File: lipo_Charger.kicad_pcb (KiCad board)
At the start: 2 copper layers, 98 parts, among them J1 Conn_01x02_Pin, J2 Conn_01x05, J3 Conn_01x04, J4 Conn_01x05, J5 Conn_01x04, Q1 NX7002AK_215(nch low power), Q2 NVTFS010N10MCLTAG(high power), Q3 NVTFS010N10MCLTAG(high power), Q4 NVTFS010N10MCLTAG(high power), Q5 NVTFS010N10MCLTAG(high power)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

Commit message: need to add stm dev boarrd and silkscreen managing sch rechecik and trace width check eed to add gnd and power plane
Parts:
- moved C24 83.7 mm to (120.6, 66.9)
- moved R4 83.7 mm to (108.5, 70.7)
- moved R40 83.7 mm to (143.1, 86.7)
- moved C1 83.7 mm to (85.9, 62.9)
- moved C15 83.7 mm to (144.8, 60.3)
- moved C16 83.7 mm to (147.9, 60.3)
- moved C18 83.7 mm to (155.0, 70.5)
- moved C2 83.7 mm to (88.9, 62.9)
- moved C21 83.7 mm to (129.7, 66.2)
- moved C22 83.7 mm to (111.5, 76.3)
- moved C23 83.7 mm to (105.1, 76.3)
- moved C27 83.7 mm to (116.2, 76.9)
- moved C3 83.7 mm to (91.9, 62.9)
- moved C33 83.7 mm to (146.2, 84.9)
- moved C4 83.7 mm to (94.9, 62.9)
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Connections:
- net Net-(Q2-Pad5-6-7-8) renamed /copper_pour1
- net Net-(U1-SW2) renamed /copper_pour2
- MOSFET2 pad 5: Net-(MOSFET2-D-Pad5) -> /copper_pour3
- Q3 pad 5-6-7-8: Net-(MOSFET2-D-Pad5) -> /copper_pour3
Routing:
- net +24V: track 40.2 -> 2.50 mm
- net /BAT: track 54.8 -> 70.8 mm
- net /copper_pour2: track 47.7 -> 37.5 mm
- net GND: track 43.5 -> 35.1 mm
- net /copper_pour1: track 9.91 -> 2.42 mm
- net Net-(MOSFET2-D-Pad5): track 5.88 -> 0.00 mm
- net /VSYS: track 39.9 -> 43.6 mm
- net /CELL_3S: track 57.7 -> 60.0 mm
- net /CELL_1S: track 69.0 -> 70.8 mm
- net /CELL_2S: track 62.4 -> 64.2 mm
- net Net-(MOSFET5-D-Pad5): track 7.35 -> 9.13 mm
- net Net-(MOSFET4-D-Pad5): track 6.75 -> 8.53 mm
- net Net-(MOSFET3-D-Pad5): track 5.65 -> 7.38 mm
- net Net-(U1-HIDRV1): track 7.70 -> 8.90 mm
- net Net-(U1-CELL_BATPRES): track 24.7 -> 23.8 mm
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- added copper zone on F.Cu, net +24V
- added copper zone on F.Cu, net /copper_pour1
- added copper zone on F.Cu, net /copper_pour2
- added copper zone on F.Cu, net /copper_pour3
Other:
- copper layers 2 -> 4

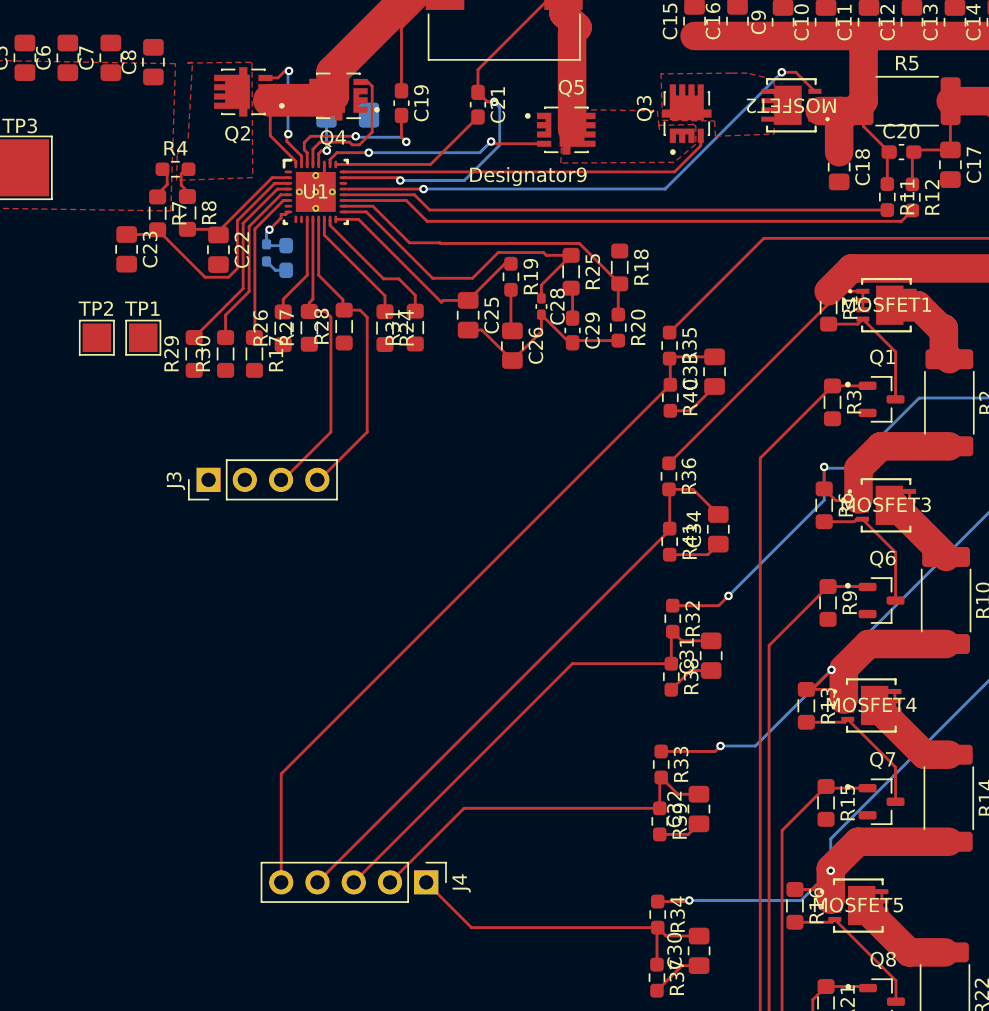
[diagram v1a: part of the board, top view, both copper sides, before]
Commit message: need to seperate analog and digital ground and reroute everything
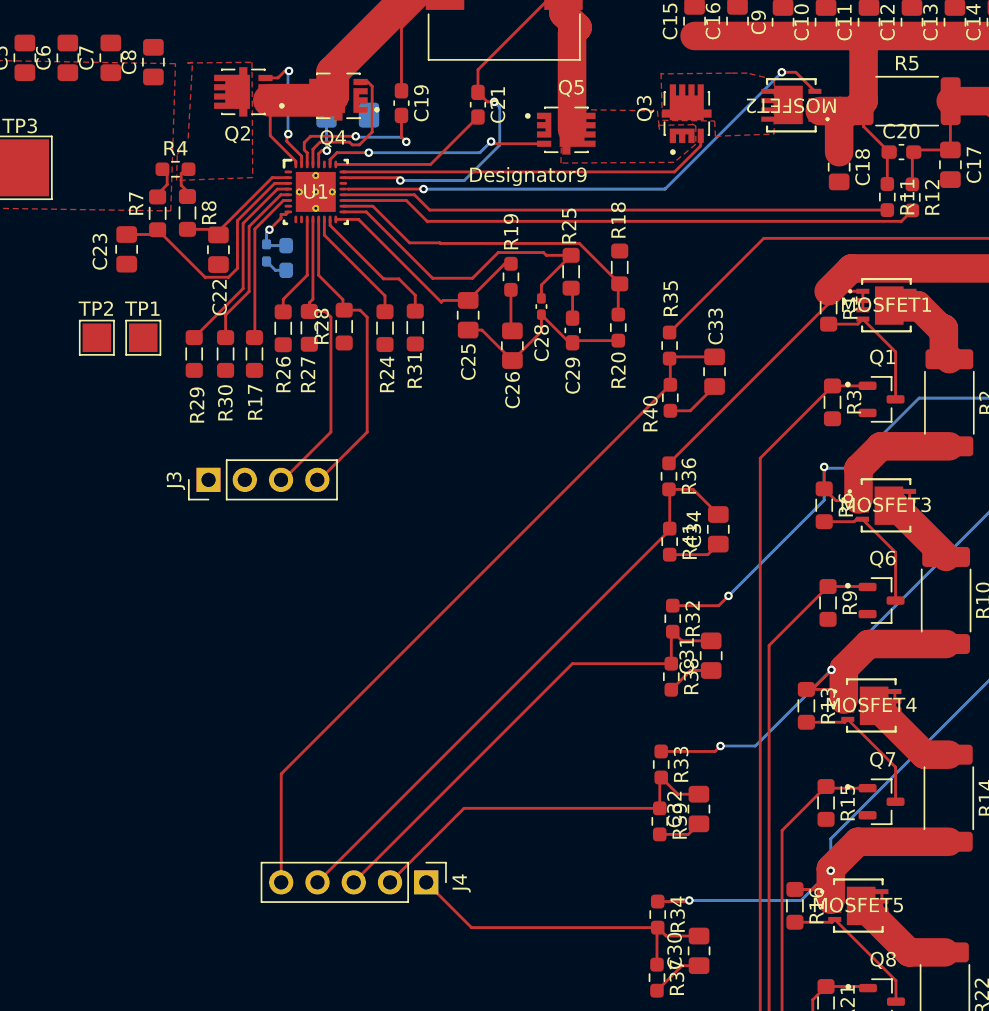
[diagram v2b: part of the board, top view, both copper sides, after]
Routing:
- net GND: track 35.1 -> 33.8 mm
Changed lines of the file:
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@@
 		(tags "inductor handsolder")
 		(property "Reference" "R30"
-			(at 0 -1.55 90)
+			(at -3.4426 0.021 90)
 			(layer "F.SilkS")
 			(effects
@@
 		)
 		(fp_text user "${REFERENCE}"
-			(at 0 0 90)
+			(at 0 0.1226 90)
 			(layer "F.Fab")
 			(effects
@@
 		(tags "inductor handsolder")
 		(property "Reference" "R18"
-			(at 0 -1.55 90)
+			(at -3.2961 0.0546 90)
 			(layer "F.SilkS")
 			(effects
@@
 		)
 		(pad "5" smd rect
-			(at 0.233775 0)
-			(size 1.92005 2.749999)
+			(at 0.2 0.025)
+			(size 2.0066 2.6924)
 			(layers "F.Cu" "F.Mask" "F.Paste")
 			(net 28 "Net-(MOSFET3-D-Pad5)")
@@
 		(tags "resistor handsolder")
 		(property "Reference" "R35"
-			(at 0 -1.43 90)
+			(at -3.2844 -0.1095 90)
 			(layer "F.SilkS")
 			(effects
@@
 		(tags "inductor handsolder")
 		(property "Reference" "R17"
-			(at 0 -1.55 90)
+			(at 3.3918 -0.0838 90)
 			(layer "F.SilkS")
 			(effects
@@
 		(tags "capacitor handsolder")
 		(property "Reference" "C28"
-			(at 0 -1.16 90)
+			(at 2.5478 -0.047 90)
 			(layer "F.SilkS")
 			(effects
@@
 		(tags "inductor handsolder")
 		(property "Reference" "R24"
-			(at 0 -1.55 90)
+			(at 3.2714 -0.1826 90)
 			(layer "F.SilkS")
 			(effects
@@
 		(tags "inductor handsolder")
 		(property "Reference" "R7"
-			(at 0 -1.55 90)
+			(at -0.6774 1.4674 90)
 			(layer "F.SilkS")
 			(effects
@@
 		(tags "capacitor handsolder")
 		(property "Reference" "C22"
-			(at 0 -1.68 90)
+			(at 3.3258 -0.1146 90)
 			(layer "F.SilkS")
 			(effects
@@
 		(tags "capacitor handsolder")
 		(property "Reference" "C26"
-			(at 0 -1.68 90)
+			(at 3.1066 -0.047 90)
 			(layer "F.SilkS")
 			(effects
@@
 		(tags "resistor handsolder")
 		(property "Reference" "R19"
-			(at 0 -1.43 90)
+			(at -3.1418 -0.047 90)
 			(layer "F.SilkS")
 			(effects
@@
 		)
 		(pad "5" smd rect
-			(at 0.233775 0)
-			(size 1.92005 2.749999)
+			(at 0.2 0.025)
+			(size 2.0066 2.6924)
 			(layers "F.Cu" "F.Mask" "F.Paste")
 			(net 30 "Net-(MOSFET4-D-Pad5)")
@@
 		(tags "inductor handsolder")
 		(property "Reference" "R31"
-			(at 0 -1.55 90)
+			(at -3.0066 -0.007 90)
 			(layer "F.SilkS")
 			(effects
@@
 		)
 		(pad "5" smd rect
-			(at 0.233775 0 180)
-			(size 1.92005 2.749999)
+			(at 0.2 0.025 180)
+			(size 2.0066 2.6924)
 			(layers "F.Cu" "F.Mask" "F.Paste")
 			(net 58 "/copper_pour3")
@@
 		(tags "inductor handsolder")
 		(property "Reference" "R25"
-			(at 0 -1.55 90)
+			(at -3.1926 0.1054 90)
 			(layer "F.SilkS")
 			(effects
@@
 		(tags "inductor handsolder")
 		(property "Reference" "R29"
-			(at 0 -1.55 90)
+			(at -3.595 0.2398 90)
 			(layer "F.SilkS")
 			(effects
@@
 		)
 		(pad "5" smd rect
-			(at 0.233775 0)
-			(size 1.92005 2.749999)
+			(at 0.2 0.025)
+			(size 2.0066 2.6924)
 			(layers "F.Cu" "F.Mask" "F.Paste")
 			(net 25 "Net-(MOSFET1-D-Pad5)")
@@
 		(tags "capacitor handsolder")
 		(property "Reference" "C23"
-			(at 0 -1.68 90)
+			(at 0.1554 1.8374 90)
 			(layer "F.SilkS")
 			(effects
@@
 		(tags "resistor handsolder")
 		(property "Reference" "R20"
-			(at 0 -1.43 90)
+			(at 3.0031 -0.047 90)
 			(layer "F.SilkS")
 			(effects
@@
 		(tags "capacitor handsolder")
 		(property "Reference" "C25"
-			(at 0 -1.68 90)
+			(at 3.259 -0.047 90)
 			(layer "F.SilkS")
 			(effects
@@
 		(tags "inductor handsolder")
 		(property "Reference" "R26"
-			(at 0 -1.55 90)
+			(at -3.259 0.047 90)
 			(layer "F.SilkS")
 			(effects
@@
 		)
 		(pad "5" smd rect
-			(at 0.233775 0)
-			(size 1.92005 2.749999)
+			(at 0.2 0.025)
+			(size 2.0066 2.6924)
 			(layers "F.Cu" "F.Mask" "F.Paste")
 			(net 31 "Net-(MOSFET5-D-Pad5)")
@@
 		(tags "inductor handsolder")
 		(property "Reference" "R27"
-			(at 0 -1.55 90)
+			(at -3.2914 -0.0546 90)
 			(layer "F.SilkS")
 			(effects
@@
 		(tags "capacitor handsolder")
 		(property "Reference" "C29"
-			(at 0 -1.43 90)
+			(at 3.1574 -0.047 90)
 			(layer "F.SilkS")
 			(effects
@@
 		(tags "capacitor handsolder")
 		(property "Reference" "C33"
-			(at 0 -1.68 90)
+			(at 3.1828 0.1095 90)
 			(layer "F.SilkS")
 			(effects
@@
 		(tags "resistor handsolder")
 		(property "Reference" "R40"
-			(at 0 -1.43 90)
+			(at 1.1352 1.3637 90)
 			(layer "F.SilkS")
 			(effects
@@
 		(width 0.2)
 		(layer "F.Cu")
-		(net 1)
-	)
-	(segment
-		(start 118.913001 70.3536)
-		(end 118.913001 71.678602)
-		(width 0.2)
-		(layer "F.Cu")

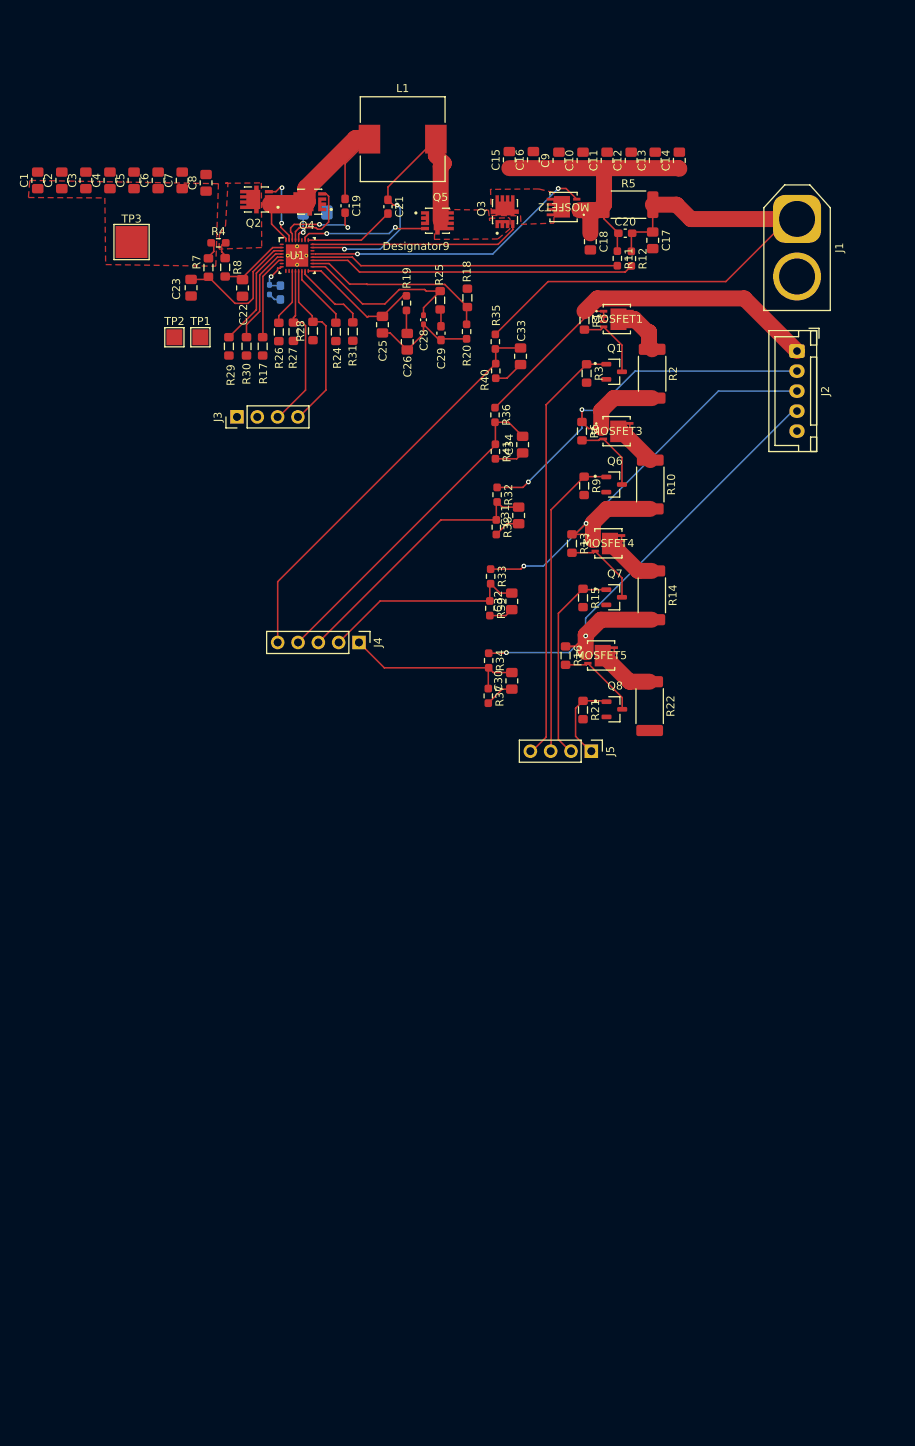
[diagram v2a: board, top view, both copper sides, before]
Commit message: all the links of the components has been assigned in the library for routing components placement is optimizes need routing
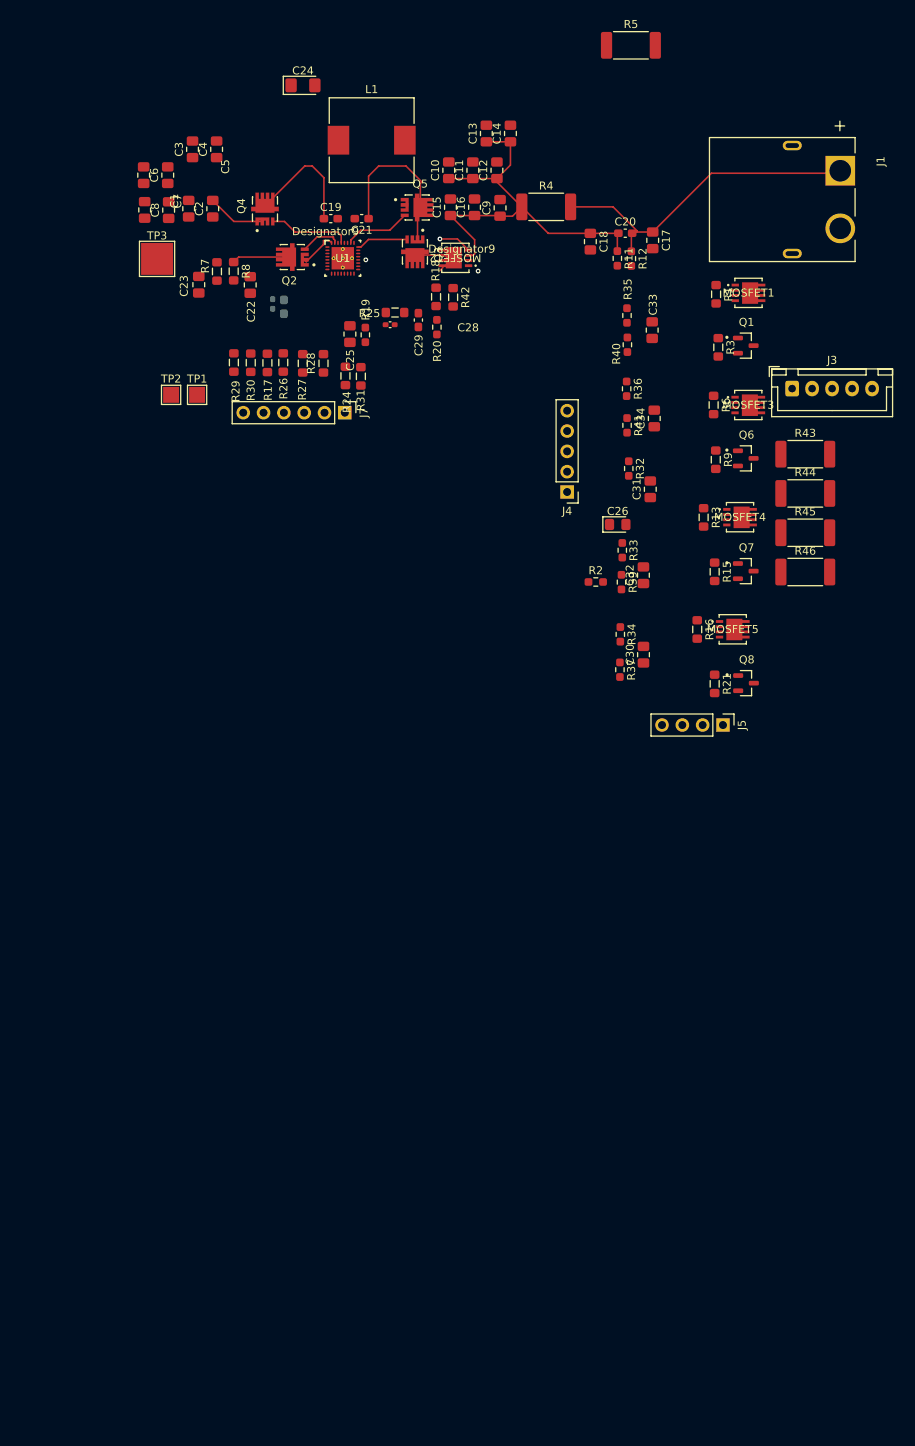
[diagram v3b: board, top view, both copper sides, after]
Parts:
- removed J2: Conn_01x05, Connector_JST:JST_XH_B5B-XH-A_1x05_P2.50mm_Vertical
- removed R10, R14, R22: R, Resistor_SMD:R_2512_6332Metric_Pad1.40x3.35mm_HandSolder
- removed R38: 8.2k, Resistor_SMD:R_0603_1608Metric_Pad0.98x0.95mm_HandSolder
- added J7: Conn_01x07, Connector_PinHeader_2.54mm:PinHeader_1x06_P2.54mm_Vertical, F.Cu at (124.3, 91.9)
- added R42: 10k, Inductor_SMD:L_0805_2012Metric_Pad1.05x1.20mm_HandSolder, F.Cu at (137.8, 77.5)
- added R43: 47ohm, Resistor_SMD:R_2512_6332Metric_Pad1.40x3.35mm_HandSolder, F.Cu at (181.8, 97.1)
- added R44: 47ohm, Resistor_SMD:R_2512_6332Metric_Pad1.40x3.35mm_HandSolder, F.Cu at (181.8, 102.0)
- added R45: 47ohm, Resistor_SMD:R_2512_6332Metric_Pad1.40x3.35mm_HandSolder, F.Cu at (181.8, 106.9)
- added R46: 47ohm, Resistor_SMD:R_2512_6332Metric_Pad1.40x3.35mm_HandSolder, F.Cu at (181.8, 111.8)
- C24: moved to F.Cu
- C26: footprint Capacitor_SMD:C_0805_2012Metric_Pad1.18x1.45mm_HandSolder -> Diode_SMD:D_0805_2012Metric_Pad1.15x1.40mm_HandSolder
- J1: value Conn_01x02_Pin -> XT60PW-M; footprint Connector_AMASS:AMASS_XT60-M_1x02_P7.20mm_Vertical -> Lipo_Charger_footprint:AMASS_XT60PW-M
- J3: value Conn_01x04 -> balance_plug_4s; footprint Connector_PinHeader_2.54mm:PinHeader_1x04_P2.54mm_Vertical -> Connector_JST:JST_XH_B5B-XH-A_1x05_P2.50mm_Vertical
- R2: value R -> 8.2k; footprint Resistor_SMD:R_2512_6332Metric_Pad1.40x3.35mm_HandSolder -> Resistor_SMD:R_0603_1608Metric_Pad0.98x0.95mm_HandSolder
- R4: value R(10ohm) -> 0.01ohm; footprint Resistor_SMD:R_0603_1608Metric_Pad0.98x0.95mm_HandSolder -> Resistor_SMD:R_2512_6332Metric_Pad1.40x3.35mm_HandSolder
- R5: value R -> 0.01ohm
- moved J3 69.5 mm to (180.2, 88.9), turned to 0 degrees
- moved R4 41.2 mm to (149.5, 66.2)
- moved C26 34.8 mm to (158.4, 105.9), turned to 0 degrees
- moved J4 32.1 mm to (152.1, 101.8), turned to 180 degrees
- moved R2 27.0 mm to (155.7, 113.1), turned to 0 degrees
- moved C13 21.4 mm to (142.0, 57.0)
- moved C14 21.4 mm to (145.0, 57.0)
- moved R5 19.9 mm to (160.0, 46.0)
- moved C1 19.2 mm to (104.8, 66.4)
- moved C2 19.2 mm to (107.8, 66.4)
- moved C11 16.8 mm to (140.3, 61.6)
- moved C12 16.8 mm to (143.3, 61.6)
- moved C10 16.8 mm to (137.3, 61.6)
- moved C30 16.8 mm to (161.6, 122.2)
- moved C33 16.8 mm to (162.7, 81.6)
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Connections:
- C22 pad 2: GND -> GNDA
- C23 pad 2: GND -> GNDA
- C24 pad 2: GND -> GNDA
- C25 pad 2: GND -> GNDA
- C26 pad 2: GND -> GNDA
- C27 pad 2: GND -> GNDA
- C28 pad 2: GND -> GNDA
- C29 pad 2: GND -> GNDA
- C31 pad 1: GND -> GNDA
- C32 pad 1: GND -> GNDA
- C33 pad 1: GND -> GNDA
- C34 pad 1: GND -> GNDA
- J3 pad 1: GND -> /CELL_4S
- J3 pad 2: VDDA -> /CELL_3S
- J3 pad 3: /SCL -> /CELL_2S
- J3 pad 4: /SDA -> /CELL_1S
- R17 pad 2: GND -> GNDA
- R2 pad 1: Net-(MOSFET1-D-Pad5) -> /CELL_3S_adc
- R2 pad 2: /CELL_3S -> GNDA
- R20 pad 2: GND -> GNDA
- R23 pad 2: GND -> GNDA
- R24 pad 2: GND -> GNDA
- R39 pad 2: GND -> GNDA
- R4 pad 1: +24V -> /VSYS
- R4 pad 2: /copper_pour1 -> /BAT
- R40 pad 2: GND -> GNDA
- R41 pad 2: GND -> GNDA
- R5 pad 1: /VSYS -> +24V
- R5 pad 2: /BAT -> /copper_pour1
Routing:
- net /CELL_1S: track 70.8 -> 0.00 mm, vias 2 -> 0
- net /CELL_2S: track 64.2 -> 0.00 mm, vias 2 -> 0
- net /CELL_3S: track 60.0 -> 0.00 mm, vias 2 -> 0
- net Net-(J5-Pin_4): track 53.9 -> 0.00 mm
- net /BAT_adc: track 51.2 -> 0.00 mm
- net /CELL_4S: track 50.3 -> 0.00 mm
- net /CELL_4S_adc: track 42.0 -> 0.00 mm
- net Net-(U1-SRN): track 40.8 -> 0.00 mm
- net Net-(J5-Pin_3): track 39.0 -> 0.00 mm
- net Net-(U1-SRP): track 38.6 -> 0.00 mm
- net /CELL_3S_adc: track 33.8 -> 0.00 mm
- net Net-(MOSFET2-G): track 36.6 -> 4.16 mm, vias 2 -> 3
- net /BAT: track 70.8 -> 43.5 mm
- net GND: track 33.8 -> 7.29 mm
- net /CELL_2S_adc: track 26.4 -> 0.00 mm
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- removed copper zone on F.Cu, net +24V
- removed copper zone on F.Cu, net /copper_pour1
- removed copper zone on F.Cu, net /copper_pour2
- removed copper zone on F.Cu, net /copper_pour3
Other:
- board text added: "Designator9"
